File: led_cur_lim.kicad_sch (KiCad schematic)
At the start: 8 parts, among them J20 TC0203620000G, K1 G5NB-1A4_DC5, K24 G5NB-1A4_DC5, Q21 BC849, Q22 BC849

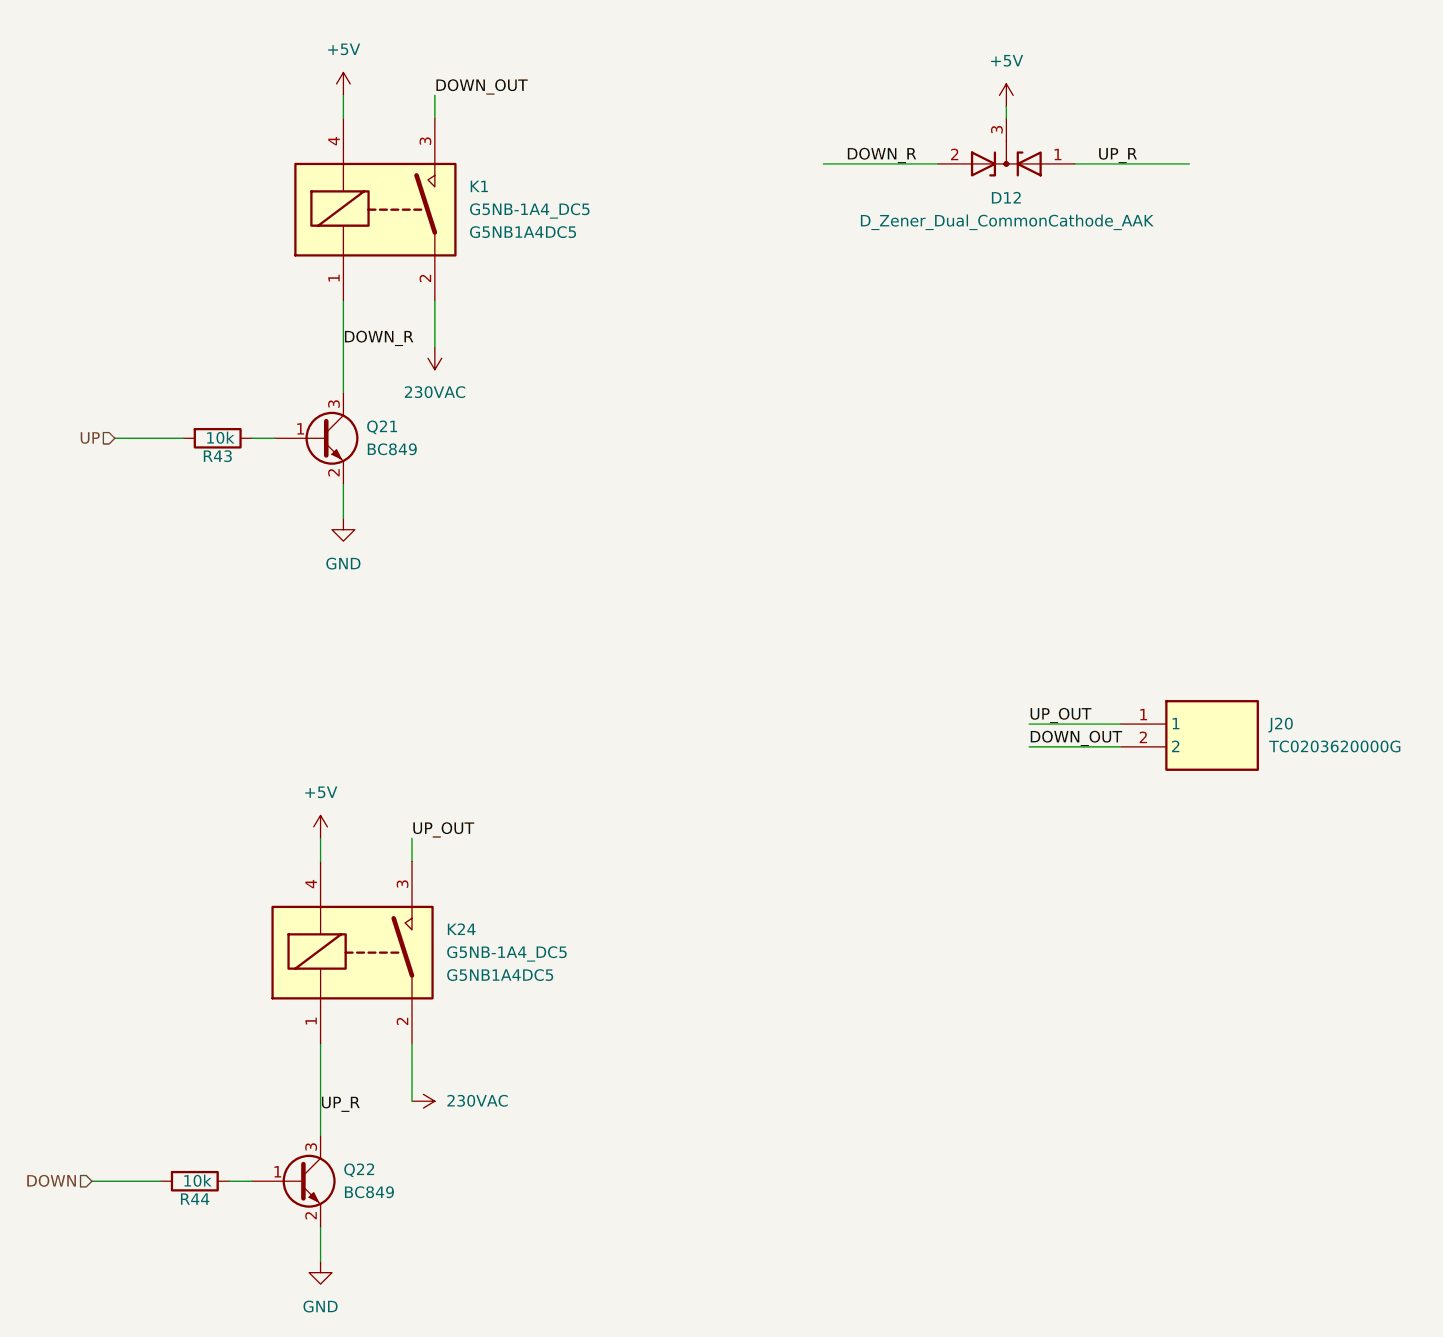
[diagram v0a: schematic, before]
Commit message: relay placment
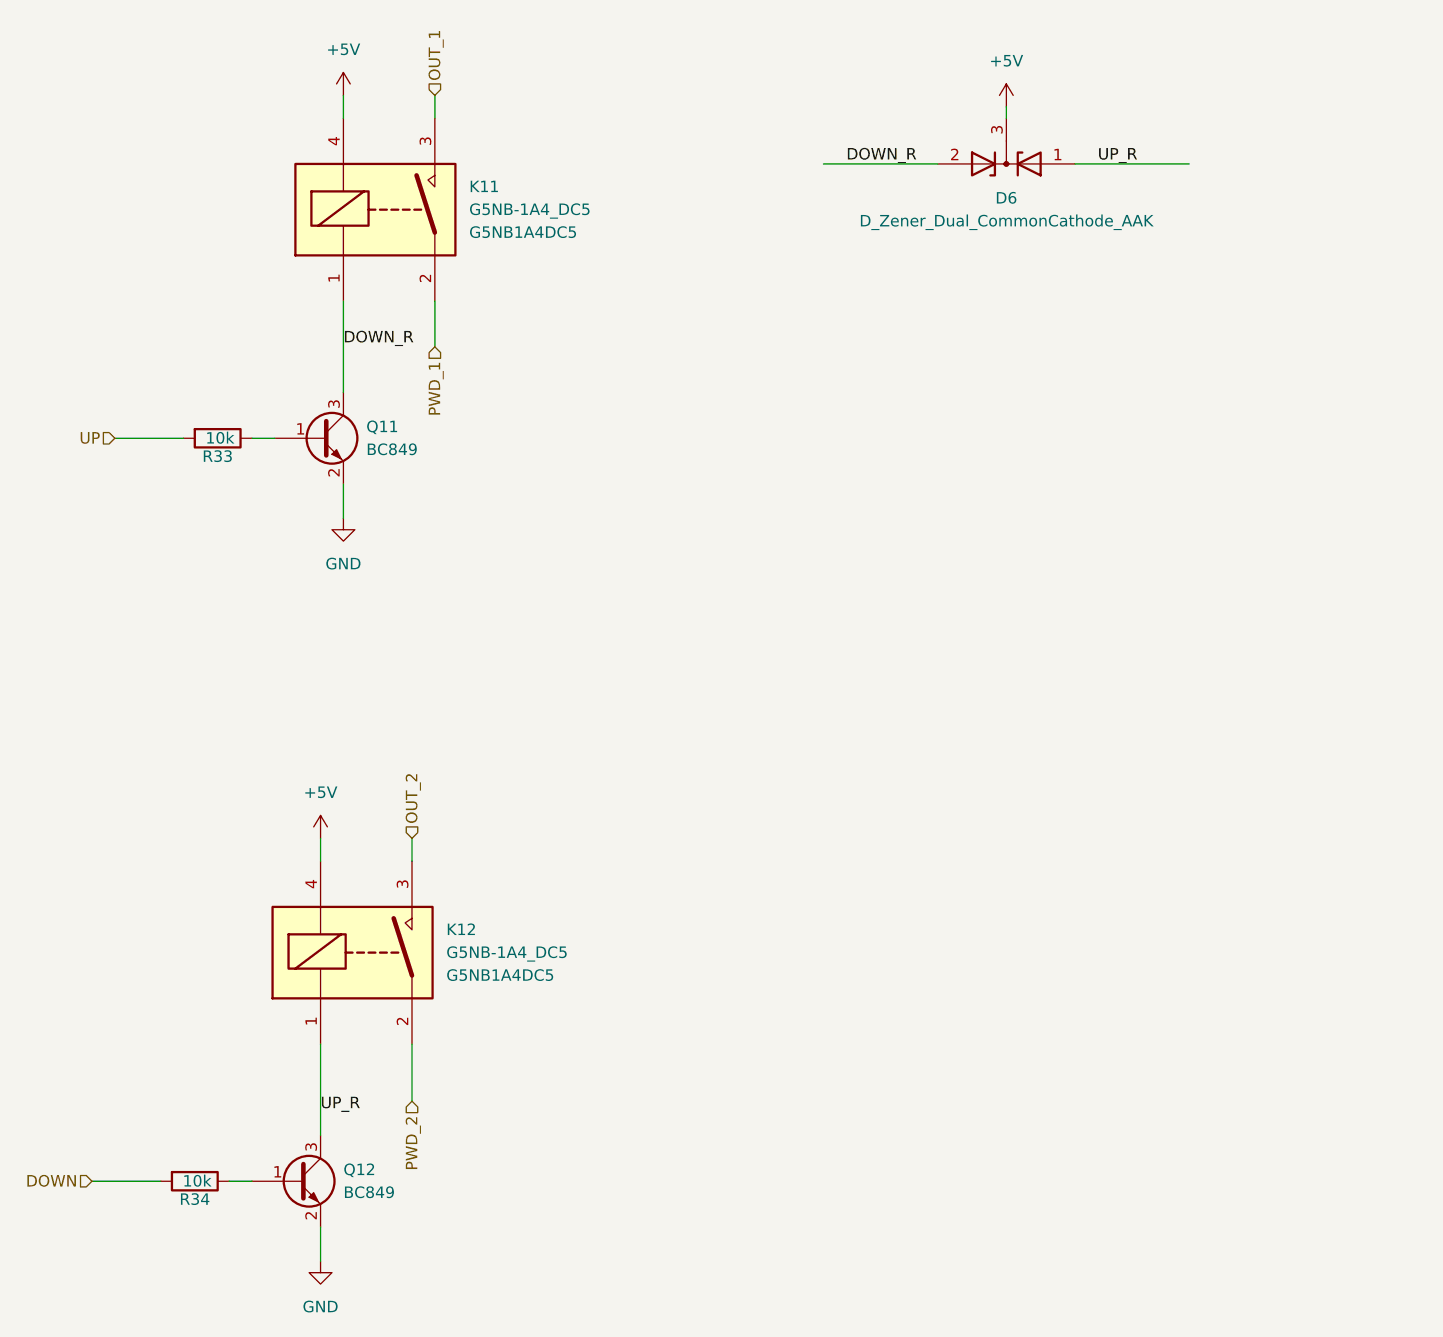
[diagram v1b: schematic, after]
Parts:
- removed J20: TC0203620000G, TC0203620000G, symbol TC0203620000G:TC0203620000G
- renumbered D12 to D6, K1 to K11, K24 to K12, Q21 to Q11, Q22 to Q12, R43 to R33, R44 to R34
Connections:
- net 230VAC renamed PWD_1
- net PWD_1: no longer K12.2
- net DOWN_OUT renamed OUT_1
- net UP_OUT renamed OUT_2
- new net PWD_2: K12.2
